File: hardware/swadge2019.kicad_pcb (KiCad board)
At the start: 2 copper layers, 78.9 x 78.6 mm, 35 parts, among them P1 PGM, P2 USBMicroB-10118194-0001LF, P3 CONN_1, P4 CONN_1, P5 CONN_1, P6 CONN_1, SW1 TACTILE, SW2 TACTILE, SW3 TACTILE, SW4 TACTILE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

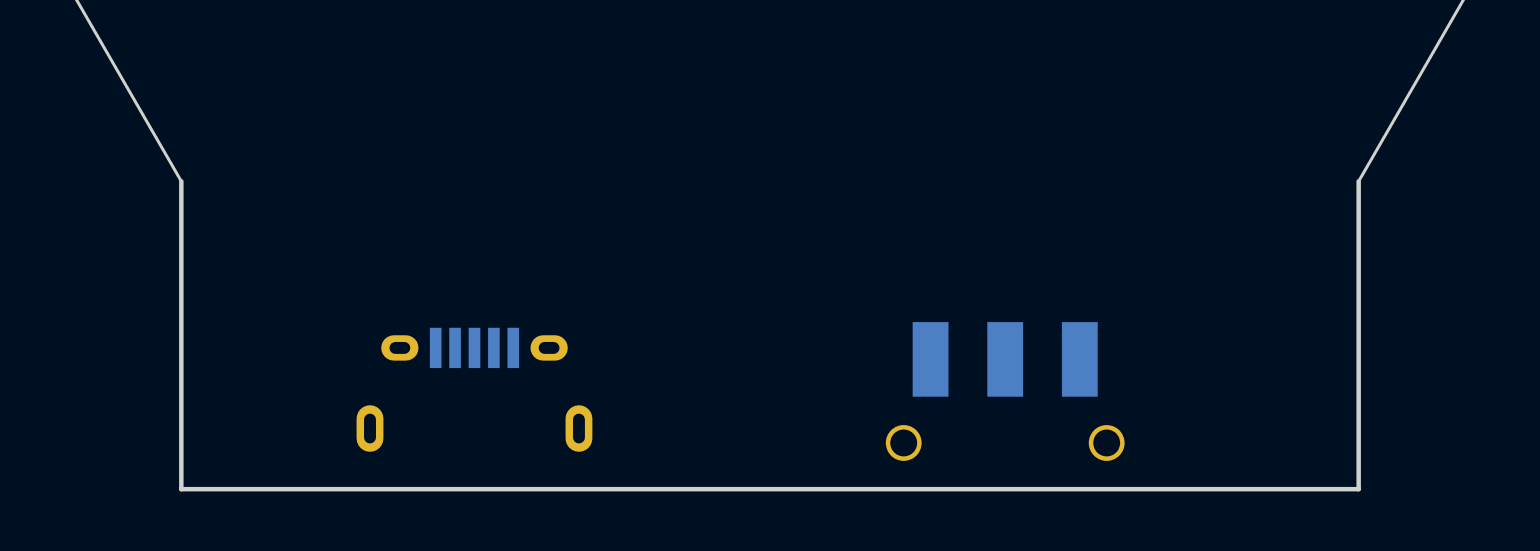
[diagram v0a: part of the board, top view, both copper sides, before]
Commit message: Fixed length of bottom pcb
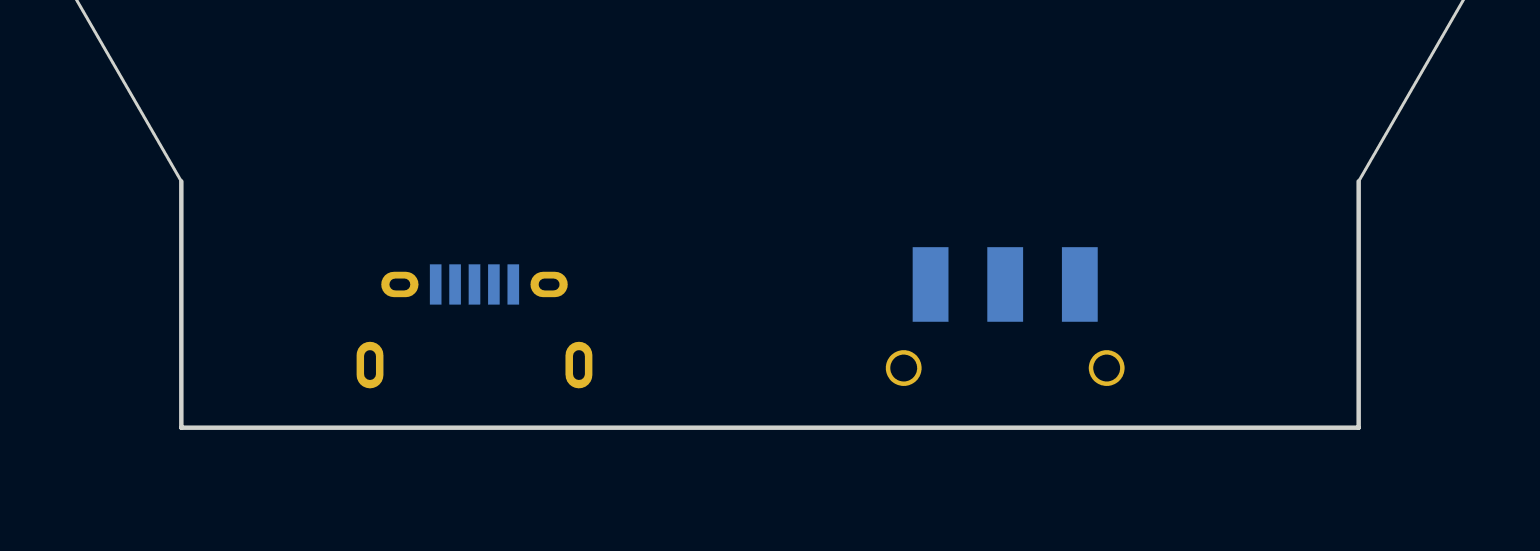
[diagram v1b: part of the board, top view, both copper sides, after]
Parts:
- moved SW7 2.51 mm to (94.5, 94.0)
- moved P2 2.13 mm to (76.7, 95.4)
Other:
- board size 78.9 x 78.6 mm -> 78.9 x 76.6 mm
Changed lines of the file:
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@@
-(kicad_pcb (version 4) (host pcbnew 4.0.2+dfsg1-stable)
+(kicad_pcb (version 20171130) (host pcbnew "(5.0.0-3-g5ebb6b6)")
   (general
-    (links 78)
-    (no_connects 78)
-    (area 47.115654 20.888155 126.100919 99.643001)
     (thickness 1.6)
     (drawings 40)
@@
       (layerselection 0x00030_80000001)
       (usegerberextensions false)
+      (usegerberattributes false)
+      (usegerberadvancedattributes false)
+      (creategerberjobfile false)
       (excludeedgelayer true)
       (linewidth 0.100000)
@@
       (hpglpennumber 1)
       (hpglpenspeed 20)
-      (hpglpendiameter 15)
-      (hpglpenoverlay 2)
+      (hpglpendiameter 15.000000)
       (psnegative false)
       (psa4output false)
@@
     (fp_line (start 0.6 0.875) (end -0.6 0.875) (layer F.SilkS) (width 0.15))
     (fp_line (start -0.6 -0.875) (end 0.6 -0.875) (layer F.SilkS) (width 0.15))
-    (pad 1 smd rect (at -0.95 0 135) (size 0.7 1.3) (layers F.Cu F.Paste F.Mask)
-      (net 1 +3V3))
-    (pad 2 smd rect (at 0.95 0 135) (size 0.7 1.3) (layers F.Cu F.Paste F.Mask)
+    (pad 1 smd rect (at -0.949999 0 135) (size 0.7 1.3) (layers F.Cu F.Paste F.Mask)
+      (net 1 +3V3))
+    (pad 2 smd rect (at 0.949999 0 135) (size 0.7 1.3) (layers F.Cu F.Paste F.Mask)
       (net 15 GPIO0))
     (model Resistors_SMD.3dshapes/R_0805.wrl
@@
     (tags "resistor 0805")
     (attr smd)
-    (fp_text reference R7 (at -3.048 -1.524 450) (layer F.SilkS)
+    (fp_text reference R7 (at -3.048 -1.524 90) (layer F.SilkS)
       (effects (font (size 1 1) (thickness 0.15)))
     )
@@
       (net 15 GPIO0))
     (model Pin_Headers.3dshapes/Pin_Header_Straight_1x05.wrl
-      (at (xyz 0 -0.2 0))
+      (offset (xyz 0 -5.079999923706055 0))
       (scale (xyz 1 1 1))
       (rotate (xyz 0 0 90))
@@
   )
   (module USBMicroB-10118194-0001LF (layer B.Cu)
-    (at 76.708 97.536 180)
+    (at 76.708 95.41 180)
     (fp_text reference P2 (at -0.00254 4.17322 180) (layer B.SilkS)
       (effects (font (size 0.762 0.762) (thickness 0.1651)) (justify mirror))
@@
   )
   (module JS_SWITCH (layer B.Cu)
-    (at 94.488 96.52 180)
+    (at 94.488 94.01 180)
     (fp_text reference SW7 (at 0 3.5 180) (layer B.SilkS)
       (effects (font (size 1 1) (thickness 0.15)) (justify mirror))
@@
     (pad 3 smd rect (at 0.575 0.5 240) (size 0.35 1) (layers F.Cu F.Paste F.Mask)
       (net 9 "Net-(D3-Pad3)"))
-    (pad 4 smd rect (at 1.4 0.5 240) (size 0.5 1) (layers F.Cu F.Paste F.Mask)
+    (pad 4 smd rect (at 1.400001 0.5 240) (size 0.5 1) (layers F.Cu F.Paste F.Mask)
       (net 2 GND))
   )
@@
       (net 1 +3V3))
     (pad 3 smd rect (at 0.575 0.5 60) (size 0.35 1) (layers F.Cu F.Paste F.Mask))
-    (pad 4 smd rect (at 1.4 0.5 60) (size 0.5 1) (layers F.Cu F.Paste F.Mask)
+    (pad 4 smd rect (at 1.400001 0.5 60) (size 0.5 1) (layers F.Cu F.Paste F.Mask)
       (net 2 GND))
   )
@@
       (effects (font (size 1 1) (thickness 0.15)))
     )
-    (fp_text value AP1117SOT223 (at -0.337997 6.984801 495) (layer F.SilkS)
+    (fp_text value AP1117SOT223 (at -0.337997 6.984801 135) (layer F.SilkS)
       (effects (font (size 1 1) (thickness 0.15)))
     )
@@
     (fp_line (start 2.032 -4.572) (end 3.556 -2.286) (layer F.SilkS) (width 0.15))
     (fp_line (start 3.556 -2.286) (end 3.556 -1.524) (layer F.SilkS) (width 0.15))
-    (pad 4 smd rect (at 0 -3.302 315) (size 3.6576 2.032) (layers F.Cu F.Paste F.Mask)
+    (pad 4 smd rect (at 0 -3.302001 315) (size 3.6576 2.032) (layers F.Cu F.Paste F.Mask)
       (net 22 "Net-(SW7-Pad3)"))
-    (pad 2 smd rect (at 0 3.302 315) (size 1.016 2.032) (layers F.Cu F.Paste F.Mask)
+    (pad 2 smd rect (at 0 3.302001 315) (size 1.016 2.032) (layers F.Cu F.Paste F.Mask)
       (net 22 "Net-(SW7-Pad3)"))
-    (pad 3 smd rect (at 2.286 3.302 315) (size 1.016 2.032) (layers F.Cu F.Paste F.Mask)
+    (pad 3 smd rect (at 2.286001 3.302 315) (size 1.016 2.032) (layers F.Cu F.Paste F.Mask)
       (net 21 +5V))
-    (pad 1 smd rect (at -2.286 3.302 315) (size 1.016 2.032) (layers F.Cu F.Paste F.Mask)
+    (pad 1 smd rect (at -2.286001 3.302 315) (size 1.016 2.032) (layers F.Cu F.Paste F.Mask)
       (net 2 GND))
     (model TO_SOT_Packages_SMD.3dshapes/SOT-223.wrl
@@
       (net 2 GND))
     (model Capacitors_ThroughHole.3dshapes/C_Radial_D8_L13_P3.8.wrl
-      (at (xyz 0.0748031 0 0))
+      (offset (xyz 1.899998711464882 0 0))
       (scale (xyz 1 1 1))
       (rotate (xyz 0 0 90))
@@
   (gr_line (start 46.556679 55.020769) (end 66.55669 20.379754) (layer F.Fab) (width 0.1))
   (gr_line (start 66.556687 89.661785) (end 46.556679 55.020769) (layer F.Fab) (width 0.1))
-  (gr_line (start 106.329604 99.568) (end 106.329604 89.25479) (angle 90) (layer Edge.Cuts) (width 0.15))
-  (gr_line (start 66.886977 99.568) (end 106.329604 99.568) (angle 90) (layer Edge.Cuts) (width 0.15))
-  (gr_line (start 66.886977 89.254792) (end 66.886977 99.568) (angle 90) (layer Edge.Cuts) (width 0.15))
+  (gr_line (start 106.329604 97.508047) (end 106.329604 89.254792) (angle 90) (layer Edge.Cuts) (width 0.15))
+  (gr_line (start 66.886977 97.508047) (end 106.329604 97.508047) (angle 90) (layer Edge.Cuts) (width 0.15))
+  (gr_line (start 66.886977 89.254792) (end 66.886977 97.508047) (angle 90) (layer Edge.Cuts) (width 0.15))
   (gr_line (start 103.806 65.714) (end 104.822 66.73) (angle 90) (layer F.SilkS) (width 0.2))
   (gr_line (start 103.806 66.73) (end 104.822 65.714) (angle 90) (layer F.SilkS) (width 0.2))

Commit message: bump design
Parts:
- added C5: .1u, C_0805, F.Cu at (73.0, 52.1)
- added C6: .1u, C_0805, F.Cu at (86.5, 76.0)
- added P10: CONN_1, 632HOLE, F.Cu at (69.8, 84.5)
- added P11: CONN_1, 632HOLE, F.Cu at (69.2, 25.4)
- added P12: CONN_1, 632HOLE, F.Cu at (103.5, 25.4)
- added P13: CONN_1, 632HOLE, F.Cu at (85.0, 44.8)
- added P7: CONN_1, 632HOLE, F.Cu at (103.5, 84.5)
- added P8: CONN_1, 632HOLE, F.Cu at (52.7, 55.2)
- added P9: CONN_1, 632HOLE, F.Cu at (120.7, 55.2)
- added R9: 1.5k, R_0805, F.Cu at (78.1, 58.5)
- P1: moved to B.Cu
- moved C1 5.30 mm to (105.1, 62.8), turned to 330 degrees
- moved R2 2.42 mm to (102.2, 65.4)
- moved U2 1.70 mm to (90.2, 68.6)
- moved R4 1.61 mm to (72.4, 67.3)
- moved SW4 1.45 mm to (75.6, 74.3)
- moved SW1 1.25 mm to (97.8, 74.3)
- turned P1 to 180 degrees
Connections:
- ESP1 pad 5: (no net) -> AUDPWR
- ESP1 pad 6: AUDPWR -> GPIO12
- ESP1 pad 7: (no net) -> GPIO13
- P2 pad 2: (no net) -> GPIO12
- P2 pad 3: (no net) -> GPIO13
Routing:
- net GND: track 0.00 -> 323.5 mm, vias 0 -> 24
- net +3V3: track 0.00 -> 224.8 mm, vias 0 -> 15
- net +5V: track 0.00 -> 106.6 mm, vias 0 -> 4
- net Net-(BT1-Pad1): track 0.00 -> 54.1 mm, vias 0 -> 1
- net GPIO12: track 0.00 -> 48.2 mm, vias 0 -> 2
- net GPIO4: track 0.00 -> 47.3 mm
- net GPIO13: track 0.00 -> 42.8 mm, vias 0 -> 1
- net GPIO0: track 0.00 -> 36.8 mm, vias 0 -> 3
- net RX: track 0.00 -> 33.6 mm, vias 0 -> 2
- net Net-(SW7-Pad3): track 0.00 -> 30.8 mm, vias 0 -> 1
- net Net-(D1-Pad3): track 0.00 -> 28.6 mm, vias 0 -> 2
- net GPIO2: track 0.00 -> 27.2 mm, vias 0 -> 2
- net Net-(D5-Pad3): track 0.00 -> 26.8 mm
- net Net-(D3-Pad3): track 0.00 -> 26.5 mm, vias 0 -> 2
- net ADCPIN: track 0.00 -> 26.2 mm
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- added copper zone on B.Cu, net GND
- added copper zone on F.Cu, net GND
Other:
- net class Default: clearance 0.2 -> 0.2159; trace_width 0.25 -> 0.381; via_drill 0.4 -> 0.35
- rule trace_clearance: 0.2 -> 0.2159

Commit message: bump design
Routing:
- net GND: track 323.5 -> 328.3 mm, vias 24 -> 25
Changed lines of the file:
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@@
   (general
     (links 93)
-    (no_connects 1)
+    (no_connects 0)
     (area 47.115654 20.888155 126.100919 97.583048)
     (thickness 1.6)
     (drawings 40)
-    (tracks 389)
+    (tracks 393)
     (zones 0)
     (modules 45)
@@
     (last_trace_width 0.381)
     (trace_clearance 0.2159)
-    (zone_clearance 0.3)
+    (zone_clearance 0.381)
     (zone_45_only yes)
     (trace_min 0.2)
@@
   (segment (start 87.65 78.12) (end 87.98 80.94) (width 0.381) (layer B.Cu) (net 0))
   (via (at 87.98 80.94) (size 0.6) (drill 0.35) (layers F.Cu B.Cu) (net 0))
-  (segment (start 77.14 58.48) (end 76.836 54.434) (width 0.381) (layer F.Cu) (net 1) (status C00000))
+  (segment (start 77.14 58.48) (end 76.836 54.434) (width 0.381) (layer F.Cu) (net 1))
   (segment (start 93.203754 87.153005) (end 104.89 79.71) (width 0.381) (layer B.Cu) (net 1))
   (segment (start 104.89 79.71) (end 110.26 71.1) (width 0.381) (layer B.Cu) (net 1))
@@
   (segment (start 68.701751 48.281751) (end 70.583365 46.027947) (width 0.381) (layer F.Cu) (net 1))
   (segment (start 70.583365 46.027947) (end 70.59 46.02) (width 0.381) (layer F.Cu) (net 1))
+  (segment (start 87.76 30.472) (end 90.7 30.01) (width 0.381) (layer F.Cu) (net 2))
+  (segment (start 90.7 30.01) (end 92.33 30.29) (width 0.381) (layer F.Cu) (net 2))
+  (via (at 92.33 30.29) (size 0.6) (drill 0.35) (layers F.Cu B.Cu) (net 2))
+  (segment (start 92.33 30.29) (end 92.33 30.12) (width 0.381) (layer B.Cu) (net 2))
   (segment (start 70.14 70.45) (end 72.84 62) (width 0.381) (layer B.Cu) (net 2))
   (via (at 72.84 62) (size 0.6) (drill 0.35) (layers F.Cu B.Cu) (net 2))
@@
   (segment (start 78.56 53.11) (end 81.92 60.92) (width 0.381) (layer B.Cu) (net 25))
   (segment (start 81.92 60.92) (end 81.03 66.11) (width 0.381) (layer B.Cu) (net 25))
-  (segment (start 79.04 58.48) (end 81.98 58.25) (width 0.381) (layer F.Cu) (net 26) (status 400000))
+  (segment (start 79.04 58.48) (end 81.98 58.25) (width 0.381) (layer F.Cu) (net 26))
   (via (at 81.98 58.25) (size 0.6) (drill 0.35) (layers F.Cu B.Cu) (net 26))
   (segment (start 81.98 58.25) (end 81.659719 58.216094) (width 0.381) (layer B.Cu) (net 26))
@@
     (min_thickness 0.254)
     (keepout (tracks not_allowed) (vias not_allowed) (copperpour allowed))
-    (fill (arc_segments 16) (thermal_gap 0.508) (thermal_bridge_width 0.508))
+    (fill yes (arc_segments 16) (thermal_gap 0.508) (thermal_bridge_width 0.508))
     (polygon
       (pts
@@
     (connect_pads (clearance 0.381))
     (min_thickness 0.254)
-    (keepout (tracks not_allowed) (vias not_allowed) (copperpour not_allowed))
-    (fill (arc_segments 16) (thermal_gap 0.508) (thermal_bridge_width 0.508))
+    (keepout (tracks allowed) (vias allowed) (copperpour not_allowed))
+    (fill yes (arc_segments 16) (thermal_gap 0.508) (thermal_bridge_width 0.508))
     (polygon
       (pts
@@
     (connect_pads (clearance 0.381))
     (min_thickness 0.254)
-    (keepout (tracks not_allowed) (vias not_allowed) (copperpour not_allowed))
-    (fill (arc_segments 16) (thermal_gap 0.508) (thermal_bridge_width 0.508))
+    (keepout (tracks allowed) (vias allowed) (copperpour not_allowed))
+    (fill yes (arc_segments 16) (thermal_gap 0.508) (thermal_bridge_width 0.508))
     (polygon
       (pts

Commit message: update for gerbers for productio
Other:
- rule pad_to_mask_clearance: 0.2 -> 0.12
- board text added: "SWADGE2019 REV - Hi, Nick."
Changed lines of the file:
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@@
     (links 93)
     (no_connects 0)
-    (area 47.115654 20.888155 126.100919 97.583048)
+    (area -37.799025 -16.142108 129.780001 101.340001)
     (thickness 1.6)
-    (drawings 40)
+    (drawings 41)
     (tracks 393)
     (zones 0)
@@
     (pad_size 4.4704 4.4704)
     (pad_drill 0)
-    (pad_to_mask_clearance 0.2)
+    (pad_to_mask_clearance 0.12)
     (aux_axis_origin 0 0)
     (grid_origin 66.28 50.54)
     (visible_elements FFFFFFFF)
     (pcbplotparams
-      (layerselection 0x00030_80000001)
-      (usegerberextensions false)
+      (layerselection 0x01038_80000001)
+      (usegerberextensions true)
       (excludeedgelayer true)
       (linewidth 0.100000)
@@
       (outputformat 1)
       (mirror false)
-      (drillshape 1)
+      (drillshape 0)
       (scaleselection 1)
-      (outputdirectory ""))
+      (outputdirectory swadge2019-rev-))
   )
   (net 0 "")
@@
       (effects (font (size 1 1) (thickness 0.15)) (justify mirror))
     )
-    (fp_text value USBMicroB-10118194-0001LF (at 0 5.588 180) (layer B.SilkS)
+    (fp_text value USBMicroB-10118194-0001LF (at -2.812 6.14 180) (layer B.SilkS)
       (effects (font (size 1 1) (thickness 0.15)) (justify mirror))
     )
@@
     )
   )
+  (gr_text "SWADGE2019\nREV -\nHi, Nick." (at 84.28 85.46) (layer F.SilkS)
+    (effects (font (size 1.5 1.5) (thickness 0.3)))
+  )
   (gr_line (start 101.556689 29.040001) (end 116.556687 55.020764) (layer F.Fab) (width 0.1))
